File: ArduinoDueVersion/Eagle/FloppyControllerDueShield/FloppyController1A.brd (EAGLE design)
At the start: 58.1 x 83.8 mm, 10 parts, among them IC2 STEPSTICK_A4988

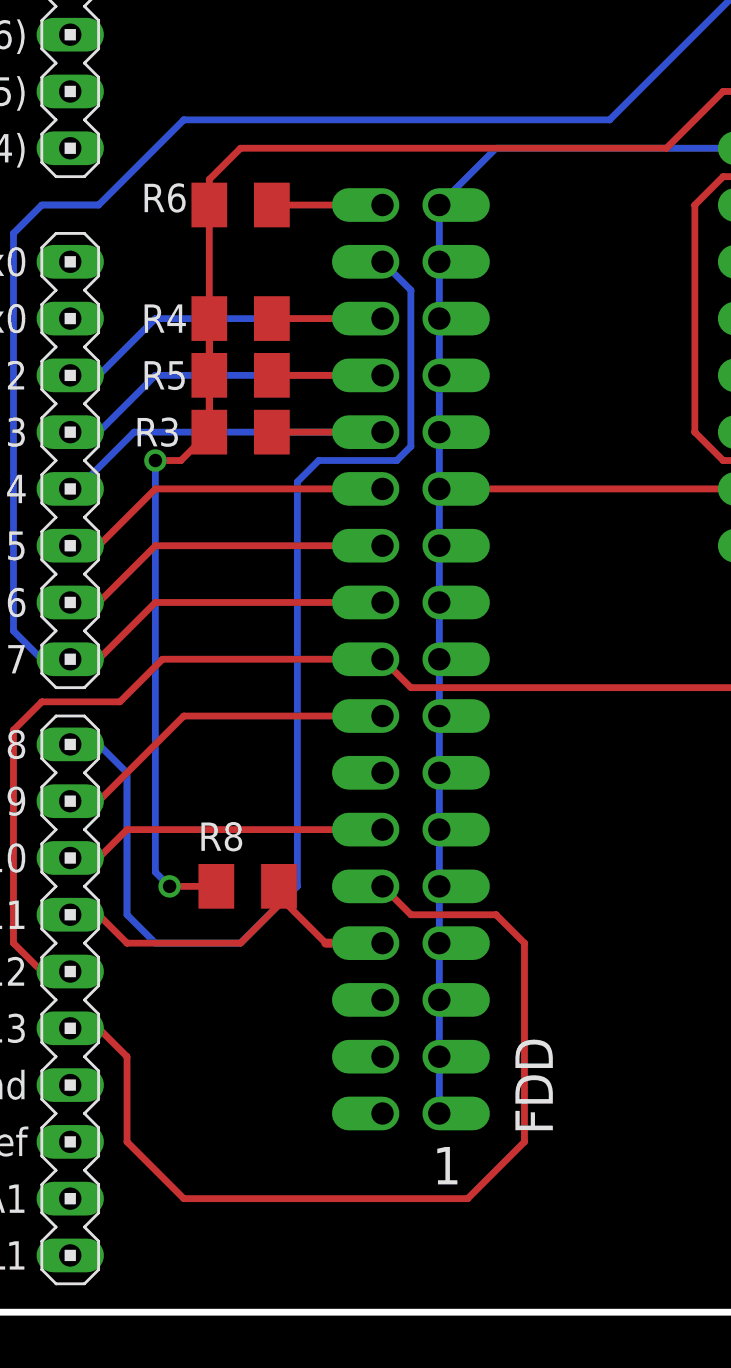
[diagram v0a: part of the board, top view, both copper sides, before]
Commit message: Tested PCB and works (stepstick needs to be tested yet), made some minor silkscreen changes. The schematic now uses 470R resistors instead of 1k. Removed some debug logging that was no longer necessary.
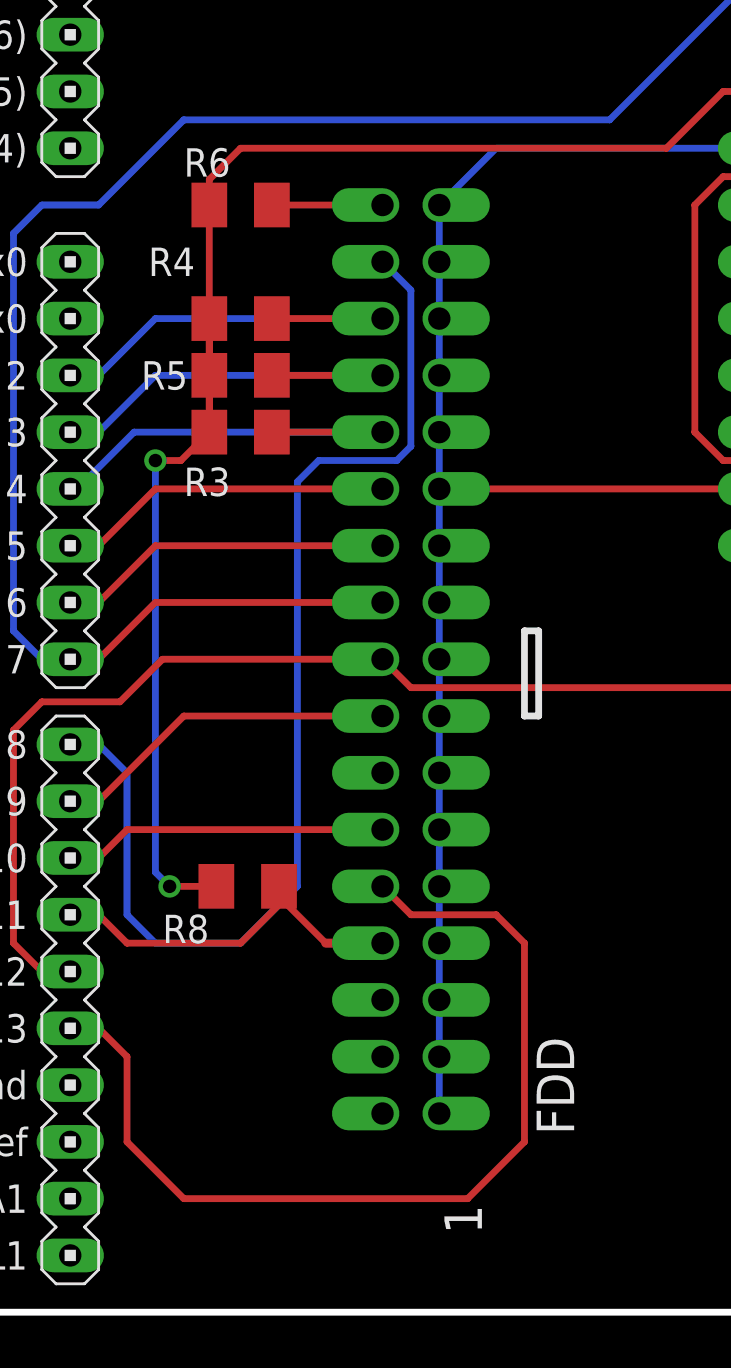
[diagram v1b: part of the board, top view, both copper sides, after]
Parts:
- R3, R4, R5, R6, R8: value 1k -> 470
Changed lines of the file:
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@@
 <grid distance="0.05" unitdist="inch" unit="inch" style="lines" multiple="1" display="no" altdistance="0.0125" altunitdist="inch" altunit="inch"/>
 <layers>
-<layer number="1" name="Top" color="4" fill="1" visible="no" active="yes"/>
-<layer number="16" name="Bottom" color="1" fill="1" visible="no" active="yes"/>
+<layer number="1" name="Top" color="4" fill="1" visible="yes" active="yes"/>
+<layer number="16" name="Bottom" color="1" fill="1" visible="yes" active="yes"/>
 <layer number="17" name="Pads" color="2" fill="1" visible="yes" active="yes"/>
 <layer number="18" name="Vias" color="2" fill="1" visible="yes" active="yes"/>
@@
 <layer number="42" name="bRestrict" color="1" fill="10" visible="no" active="yes"/>
 <layer number="43" name="vRestrict" color="2" fill="10" visible="no" active="yes"/>
-<layer number="44" name="Drills" color="7" fill="1" visible="yes" active="yes"/>
-<layer number="45" name="Holes" color="7" fill="1" visible="yes" active="yes"/>
+<layer number="44" name="Drills" color="7" fill="1" visible="no" active="yes"/>
+<layer number="45" name="Holes" color="7" fill="1" visible="no" active="yes"/>
 <layer number="46" name="Milling" color="3" fill="1" visible="no" active="yes"/>
 <layer number="47" name="Measures" color="7" fill="1" visible="no" active="yes"/>
@@
 <text x="47.9425" y="31.115" size="1.6764" layer="25">1</text>
 <text x="55.88" y="8.5725" size="1.4224" layer="21" rot="R180">GND</text>
-<text x="21.2725" y="5.715" size="1.6764" layer="25">1</text>
+<text x="23.495" y="3.4925" size="1.6764" layer="25" rot="R90">1</text>
+<wire x1="25.4" y1="30.48" x2="25.4" y2="26.67" width="0.3048" layer="21"/>
+<wire x1="25.4" y1="26.67" x2="26.035" y2="26.67" width="0.3048" layer="21"/>
+<wire x1="26.035" y1="26.67" x2="26.035" y2="30.48" width="0.3048" layer="21"/>
+<wire x1="26.035" y1="30.48" x2="25.4" y2="30.48" width="0.3048" layer="21"/>
 </plain>
 <attributes>
@@
 <elements>
 <element name="FDD" library="_MyComponents" package="FLOPPY_34PIN_DUALROW" value="FLOPPY_34PIN_CONN" x="21.59" y="8.89" smashed="yes" rot="R180">
-<attribute name="NAME" x="26.67" y="7.9375" size="1.6764" layer="21" rot="R90"/>
+<attribute name="NAME" x="27.6225" y="7.9375" size="1.6764" layer="21" rot="R90"/>
 </element>
 <element name="IC2" library="_MyComponents" package="STEPSTICK_A4988" value="STEPSTICK_A4988" x="48.26" y="34.29" smashed="yes" rot="R180">
 <attribute name="NAME" x="46.99" y="33.02" size="1.27" layer="21" rot="R180"/>
 </element>
-<element name="R3" library="rcl" package="M1206" value="1k" x="12.7" y="39.37" smashed="yes" rot="R180">
-<attribute name="NAME" x="7.9375" y="38.735" size="1.27" layer="25"/>
-<attribute name="VALUE" x="14.9225" y="39.0525" size="1.27" layer="27"/>
-</element>
-<element name="R4" library="rcl" package="M1206" value="1k" x="12.7" y="44.45" smashed="yes" rot="R180">
-<attribute name="NAME" x="8.255" y="43.815" size="1.27" layer="25"/>
-<attribute name="VALUE" x="14.9225" y="44.1325" size="1.27" layer="27"/>
-</element>
-<element name="R6" library="rcl" package="M1206" value="1k" x="12.7" y="49.53" smashed="yes" rot="R180">
-<attribute name="NAME" x="8.255" y="49.2125" size="1.27" layer="25"/>
-<attribute name="VALUE" x="14.9225" y="49.2125" size="1.27" layer="27"/>
-</element>
-<element name="R8" library="rcl" package="M1206" value="1k" x="13.0175" y="19.05" smashed="yes" rot="R180">
-<attribute name="NAME" x="10.795" y="20.6375" size="1.27" layer="25"/>
-<attribute name="VALUE" x="15.24" y="18.415" size="1.27" layer="27"/>
+<element name="R3" library="rcl" package="M1206" value="470" x="12.7" y="39.37" smashed="yes" rot="R180">
+<attribute name="NAME" x="10.16" y="36.5125" size="1.27" layer="25"/>
+<attribute name="VALUE" x="13.0175" y="36.5125" size="1.27" layer="27"/>
+</element>
+<element name="R4" library="rcl" package="M1206" value="470" x="12.7" y="44.45" smashed="yes" rot="R180">
+<attribute name="NAME" x="8.5725" y="46.355" size="1.27" layer="25"/>
+<attribute name="VALUE" x="7.62" y="44.7675" size="1.27" layer="27"/>
+</element>
+<element name="R6" library="rcl" package="M1206" value="470" x="12.7" y="49.53" smashed="yes" rot="R180">
+<attribute name="NAME" x="10.16" y="50.8" size="1.27" layer="25"/>
+<attribute name="VALUE" x="13.335" y="50.8" size="1.27" layer="27"/>
+</element>
+<element name="R8" library="rcl" package="M1206" value="470" x="13.0175" y="19.05" smashed="yes" rot="R180">
+<attribute name="NAME" x="9.2075" y="16.51" size="1.27" layer="25"/>
+<attribute name="VALUE" x="9.2075" y="14.9225" size="1.27" layer="27"/>
 </element>
 <element name="SL5" library="con-amp-quick" package="04P" value="Stepper motor" x="41.91" y="57.15" smashed="yes" rot="R180">
@@
 <attribute name="MPN" value="" x="50.8" y="3.81" size="1.778" layer="27" display="off"/>
 </element>
-<element name="R5" library="rcl" package="M1206" value="1k" x="12.7" y="41.91" smashed="yes" rot="R180">
+<element name="R5" library="rcl" package="M1206" value="470" x="12.7" y="41.91" smashed="yes" rot="R180">
 <attribute name="NAME" x="8.255" y="41.275" size="1.27" layer="25"/>
-<attribute name="VALUE" x="14.9225" y="41.5925" size="1.27" layer="27"/>
+<attribute name="VALUE" x="7.62" y="39.6875" size="1.27" layer="27"/>
 </element>
 <element name="U$1" library="DUElib130425" package="DUE(NORMAL_NO_CONN)" value="DUE(NOCONN)" x="27.94" y="38.1" rot="R90"/>
